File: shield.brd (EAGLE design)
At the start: 87.6 x 65.4 mm, 14 parts, among them X1 22-03-5035, X2 22-03-5035, Y1 22-03-5035, Y2 22-03-5035

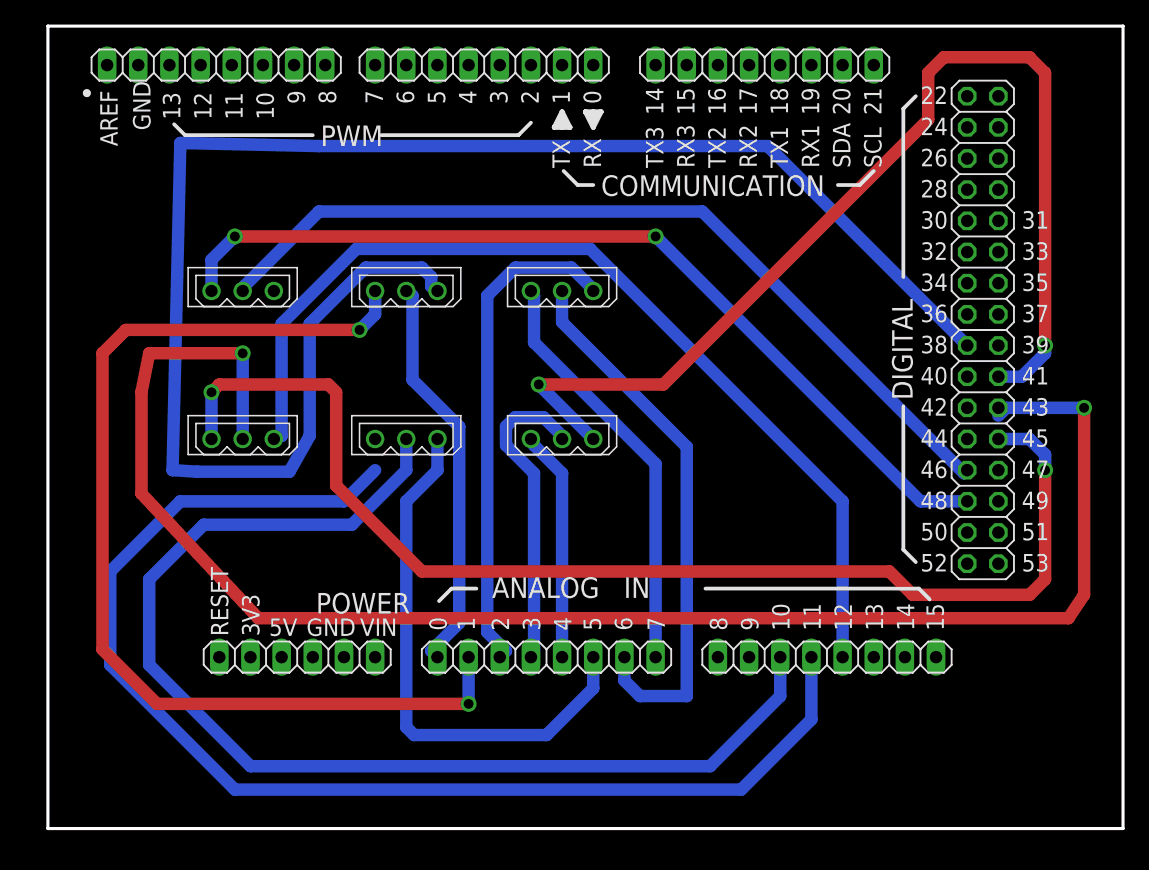
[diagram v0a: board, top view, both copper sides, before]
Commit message: change to 4 pin header
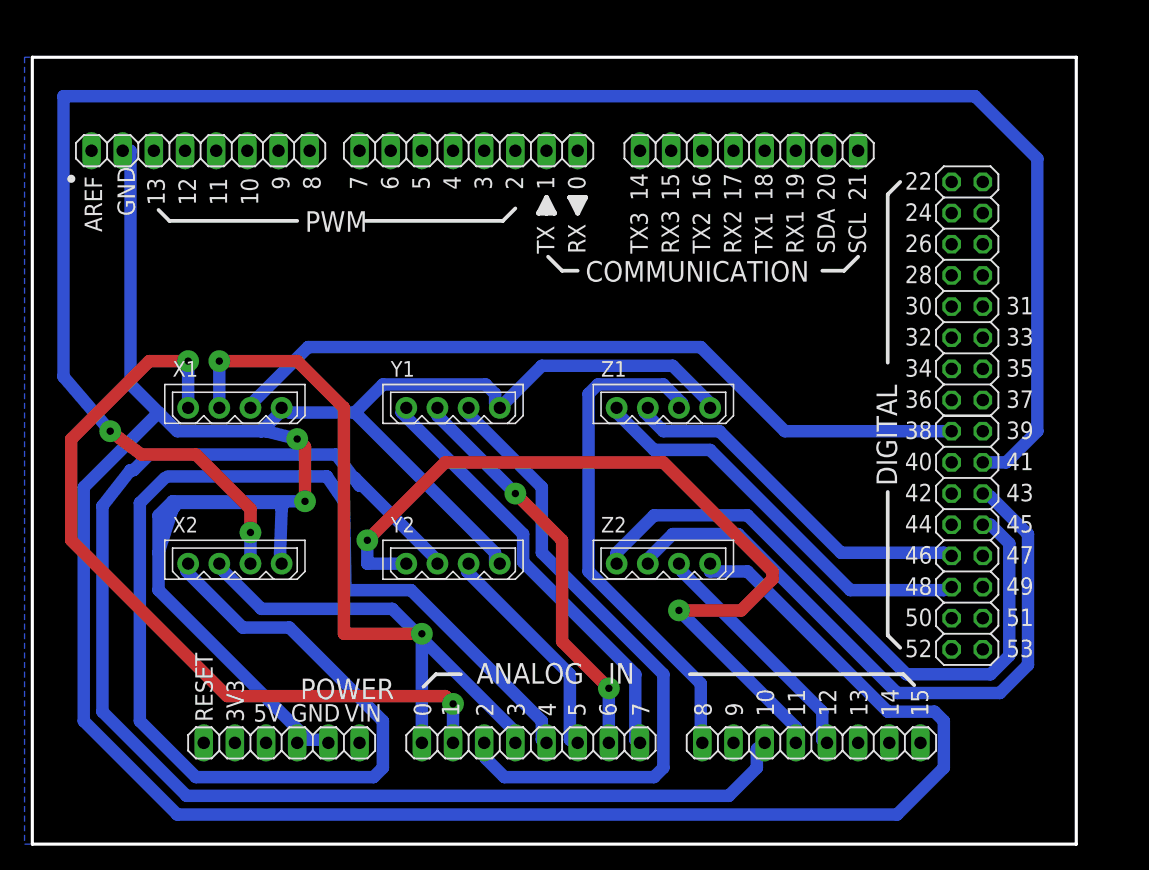
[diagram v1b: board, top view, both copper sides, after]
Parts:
- X1, X2, Y1, Y2, Z1, Z2: value 22-03-5035 -> 22-03-5045; device molex:5267-3 -> molex:5267-4
- moved Z2 37.0 mm to (55.9, 24.1)
- moved Z1 36.8 mm to (55.9, 36.8)
- moved X2 27.4 mm to (21.0, 24.1)
- moved X1 15.9 mm to (21.0, 36.8)
- moved Y1 12.2 mm to (38.7, 36.8)
- moved Y2 11.4 mm to (38.7, 24.1)
- moved XIOH 7.10 mm to (76.8, 46.4)
- moved XIOL 7.10 mm to (76.8, 26.0)
- moved ADCL 7.10 mm to (41.3, 9.53)
- moved POWER 7.10 mm to (21.0, 9.53)
- moved ADCH 7.10 mm to (64.1, 9.53)
- moved COMMUNICATION 7.10 mm to (59.1, 57.8)
- moved PWML 7.10 mm to (36.2, 57.8)
- moved PWMH 7.10 mm to (14.4, 57.8)
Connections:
- removed net ADC8: ADCH.1
- removed net N$1: POWER.5
- removed net N$2: POWER.4
- net GND: now also POWER.4, POWER.5, X1.1, X2.1, Y1.1, Y2.1, Z1.1, Z2.1
- net X1DIR: now also X1.4; no longer X1.3
- net X1EN: now also X1.2; no longer X1.1
- net X1STEP: now also X1.3; no longer X1.2
- net X2DIR: now also X2.4; no longer X2.3
- net X2EN: now also X2.2; no longer X2.1
- net X2STEP: now also X2.3; no longer X2.2
- net Y1DIR: now also Y1.4; no longer Y1.3
- net Y1EN: now also Y1.2; no longer Y1.1
- net Y1STEP: now also Y1.3; no longer Y1.2
- net Y2DIR: now also Y2.4; no longer Y2.3
- net Y2EN: now also Y2.2; no longer Y2.1
- net Y2STEP: now also Y2.3; no longer Y2.2
- net Z1DIR: now also Z1.4; no longer Z1.3
- net Z1EN: now also ADCH.1, Z1.2; no longer Z1.1
- net Z1STEP: now also Z1.3; no longer Z1.2
- net Z2DIR: now also Z2.4; no longer Z2.3
- net Z2EN: now also Z2.2; no longer Z2.1
- net Z2STEP: now also Z2.3; no longer Z2.2
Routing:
- net GND: track 0.00 -> 289.7 mm, vias 0 -> 2
- net X2DIR: track 18.8 -> 113.2 mm
- net Z2STEP: track 130.8 -> 54.4 mm, vias 2 -> 0
- net X1EN: track 133.1 -> 62.2 mm
- net X2EN: track 88.8 -> 156.3 mm
- net Z2EN: track 79.3 -> 19.6 mm
- net Z2DIR: track 98.6 -> 52.1 mm, vias 2 -> 0
- net Z1EN: track 0.00 -> 41.3 mm
- net Z1STEP: track 70.8 -> 30.3 mm
- net Z1DIR: track 73.9 -> 33.7 mm, vias 2 -> 0
- net Y2DIR: track 101.4 -> 68.5 mm, vias 0 -> 2
- net Y2EN: track 44.2 -> 18.5 mm
- net X1DIR: track 85.1 -> 64.0 mm
- net Y2STEP: track 94.6 -> 111.0 mm
- net X1STEP: track 32.8 -> 49.2 mm, vias 0 -> 2
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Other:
- board size 87.6 x 65.4 mm -> 85.1 x 64.1 mm
